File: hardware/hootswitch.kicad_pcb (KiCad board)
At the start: 2 copper layers, 100 x 88 mm, 137 parts, among them J1 Mini-DIN-4-G, J2 Switch1, J3 Mini-DIN-4-G, J4 Mini-DIN-4-G, J5 Mini-DIN-4-G, J6 Mini-DIN-4-G, J7 Barrel_Jack_MountingPin, J8 POWER, J9 POWSEL, Q1 MMBT3904, Q10 MMBT3904, Q11 MMBT3904, Q12 MMBT3904, Q13 MMBT3904, Q14 MMBT3904, Q15 MMBT3904, Q16 MMBT3904, Q17 MMBT3904, Q18 MMBT3904, Q19 MMBT3904, Q2 MMBT3904, Q20 MMBT3904, Q21 MMBT3906, Q22 MMBT3906, Q23 MMBT3906, Q24 MMBT3906, Q3 MMBT3904, Q4 MMBT3904, Q5 MMBT3904, Q6 MMBT3904, Q7 MMBT3904, Q8 MMBT3904, Q9 MMBT3904, SW1 Switch1, U1 Pico, U10 LTV-357T, U11 LTV-357T, U12 LTV-357T, U13 LTV-357T, U14 LM1117-5.0, U2 LTV-357T, U3 LTV-357T, U4 LTV-357T, U5 LTV-357T, U6 LTV-357T, U7 LTV-357T, U8 LTV-357T, U9 LTV-357T

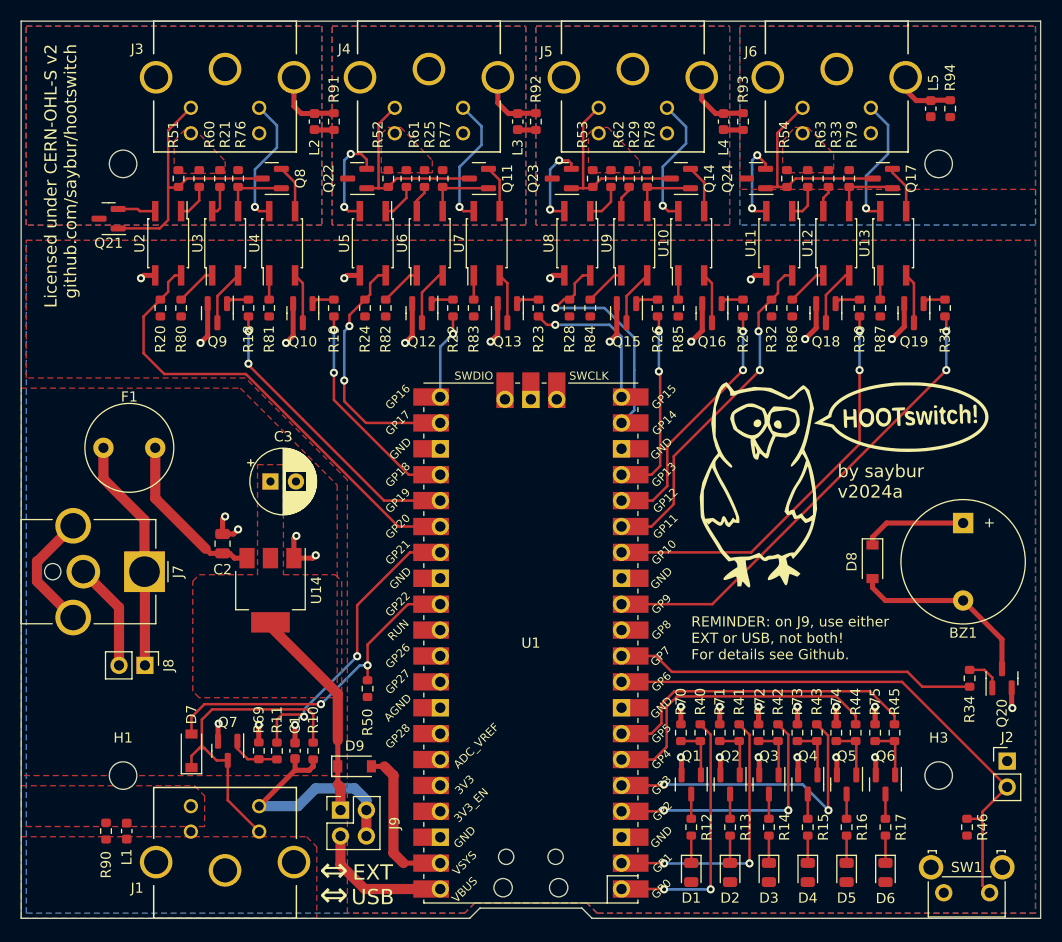
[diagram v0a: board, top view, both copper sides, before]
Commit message: Switch to using proper digital isolator for data lines.
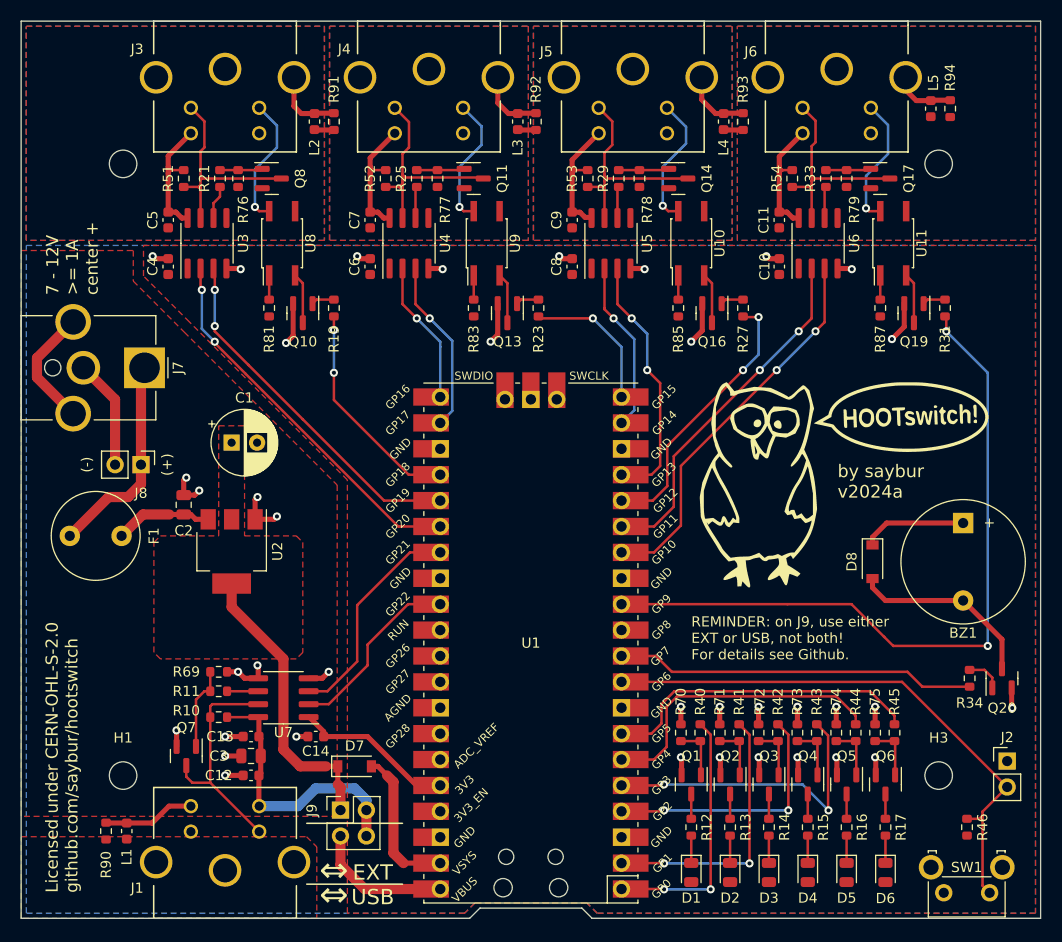
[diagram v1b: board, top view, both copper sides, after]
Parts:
- removed the D7 at (76.7, 131.6)
- removed Q12, Q15, Q18, Q9: MMBT3904, Package_TO_SOT_SMD:SOT-23
- removed Q21, Q22, Q23, Q24: MMBT3906, Package_TO_SOT_SMD:SOT-23
- removed R18, R20, R22, R24, R26, R28, R30, R32: 1K, Resistor_SMD:R_0603_1608Metric
- removed R50: 4K7, Resistor_SMD:R_0603_1608Metric
- removed R60, R61, R62, R63: 470, Resistor_SMD:R_0603_1608Metric
- removed R80, R82, R84, R86: 330, Resistor_SMD:R_0603_1608Metric
- removed the U11 at (134.4, 81.8)
- removed U12: LTV-357T, Package_SO:SO-4_4.4x3.6mm_P2.54mm
- removed the U2 at (74.4, 81.8)
- removed the U8 at (114.6, 81.8)
- removed the U9 at (120.1, 81.8)
- added C10: 100nF, Capacitor_SMD:C_0603_1608Metric, F.Cu at (134.4, 84.1)
- added C11: 100nF, Capacitor_SMD:C_0603_1608Metric, F.Cu at (134.4, 79.5)
- added C13: 100nF, Capacitor_SMD:C_0603_1608Metric, F.Cu at (82.5, 130.2)
- added C14: 100nF, Capacitor_SMD:C_0603_1608Metric, F.Cu at (88.9, 130.2)
- added C3: 10uF, Capacitor_SMD:C_0805_2012Metric, F.Cu at (82.5, 132.1)
- added C4: 100nF, Capacitor_SMD:C_0603_1608Metric, F.Cu at (74.4, 84.1)
- added C5: 100nF, Capacitor_SMD:C_0603_1608Metric, F.Cu at (74.4, 79.5)
- added C6: 100nF, Capacitor_SMD:C_0603_1608Metric, F.Cu at (94.2, 84.1)
- added C7: 100nF, Capacitor_SMD:C_0603_1608Metric, F.Cu at (94.2, 79.5)
- added C8: 100nF, Capacitor_SMD:C_0603_1608Metric, F.Cu at (114.0, 84.1)
- added C9: 100nF, Capacitor_SMD:C_0603_1608Metric, F.Cu at (114.0, 79.5)
- added U4: ADuM1201AR, Package_SO:SOIC-8_3.9x4.9mm_P1.27mm, F.Cu at (98.0, 81.8)
- added U7: ADuM1201AR, Package_SO:SOIC-8_3.9x4.9mm_P1.27mm, F.Cu at (85.7, 126.4)
- D8: value 1N4148W -> B5819W
- U3, U5, U6: value LTV-357T -> ADuM1201AR; footprint Package_SO:SO-4_4.4x3.6mm_P2.54mm -> Package_SO:SOIC-8_3.9x4.9mm_P1.27mm
- moved U6 38.1 mm to (138.2, 81.8)
- moved U5 23.4 mm to (117.9, 81.8), turned to 90 degrees
- moved J7 20.0 mm to (72.1, 94.0)
- moved J8 19.7 mm to (71.8, 103.5)
- moved R10 9.85 mm to (79.4, 128.3), turned to 180 degrees
- moved F1 9.25 mm to (64.8, 110.5)
- moved R69 8.69 mm to (79.4, 123.8), turned to 0 degrees
- moved R11 8.18 mm to (79.4, 125.7), turned to 180 degrees
- moved C1 5.39 mm to (80.6, 101.3)
- moved C2 5.39 mm to (75.9, 107.4)
- moved U2 5.39 mm to (80.6, 112.0)
- moved C12 4.95 mm to (82.5, 134.0), turned to 180 degrees
- moved Q7 4.10 mm to (76.2, 132.1)
- moved U3 1.78 mm to (78.2, 81.8)
- moved R29 1.02 mm to (118.6, 75.4)
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- renumbered C3 to C1, C1 to C12, D9 to D7, U13 to U11, U14 to U2, U4 to U8, U7 to U9
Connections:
- R11 pad 1: /A_DO -> Net-(U7-Pad6)
- R21 pad 2: Net-(J3-Pad3) -> Net-(Q8-Pad1)
- R25 pad 2: Net-(J4-Pad3) -> Net-(Q11-Pad1)
- R29 pad 2: Net-(J5-Pad3) -> Net-(Q14-Pad1)
- R33 pad 2: Net-(J6-Pad3) -> Net-(Q17-Pad1)
- U1 pad 21: /C2_DO -> /C2_DI
- U1 pad 22: /C2_DI -> /C2_DO
- U3 pad 1: Net-(R80-Pad1) -> +3.3V
- U3 pad 2: Net-(Q9-Pad3) -> /C1_DI
- U3 pad 3: Net-(Q8-Pad1) -> /C1_DO
- U3 pad 4: Net-(R21-Pad1) -> GND
- U5 pad 1: Net-(R61-Pad1) -> +3.3V
- U5 pad 2: Net-(Q22-Pad2) -> /C3_DI
- U5 pad 3: GND -> /C3_DO
- U5 pad 4: /C2_DI -> GND
- U6 pad 1: Net-(R82-Pad1) -> +3.3V
- U6 pad 2: Net-(Q12-Pad3) -> /C4_DI
- U6 pad 3: Net-(Q11-Pad1) -> /C4_DO
- U6 pad 4: Net-(R25-Pad1) -> GND
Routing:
- net /C4_PSW: track 46.7 -> 71.7 mm
- net +3.3V: track 10.2 -> 26.2 mm
- net /A_DI: track 33.3 -> 18.2 mm, vias 2 -> 0
- net Net-(J5-Pad3): track 0.00 -> 13.1 mm
- net Net-(J4-Pad3): track 0.00 -> 13.0 mm
- net Net-(J3-Pad3): track 0.00 -> 12.9 mm
- net Net-(J6-Pad3): track 0.00 -> 12.7 mm
- net /C2_DI: track 24.8 -> 14.1 mm, vias 2 -> 1
- net Net-(Q22-Pad2): track 9.87 -> 0.00 mm, vias 2 -> 0
- net Net-(J1-Pad4): track 0.00 -> 9.03 mm
- net /C2_DO: track 8.43 -> 17.1 mm
- net Net-(Q24-Pad2): track 8.60 -> 0.00 mm, vias 2 -> 0
- net Net-(U7-Pad7): track 31.3 -> 22.8 mm
- net Net-(Q23-Pad2): track 8.50 -> 0.00 mm, vias 2 -> 0
- net /C1_DI: track 45.7 -> 37.5 mm, vias 0 -> 2
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- removed copper zone on F.Cu, net Net-(J1-Pad4)
- removed copper zone on F.Cu, net Net-(J3-Pad3)
- removed copper zone on F.Cu, net Net-(J4-Pad3)
- removed copper zone on F.Cu, net Net-(J5-Pad3)
- removed copper zone on F.Cu, net Net-(J6-Pad3)
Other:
- board text added: "(+)"
- board text added: "(-)"
- board text added: "7 - 12V >= 1A center +"
- board text added: "Licensed under CERN-OHL-S-2.0 github.com/saybur/hootswitch"
- board text removed: "Licensed under CERN-OHL-S v2 github.com/saybur/hootswitch"

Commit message: Refinements for v2024a during BOM creation.
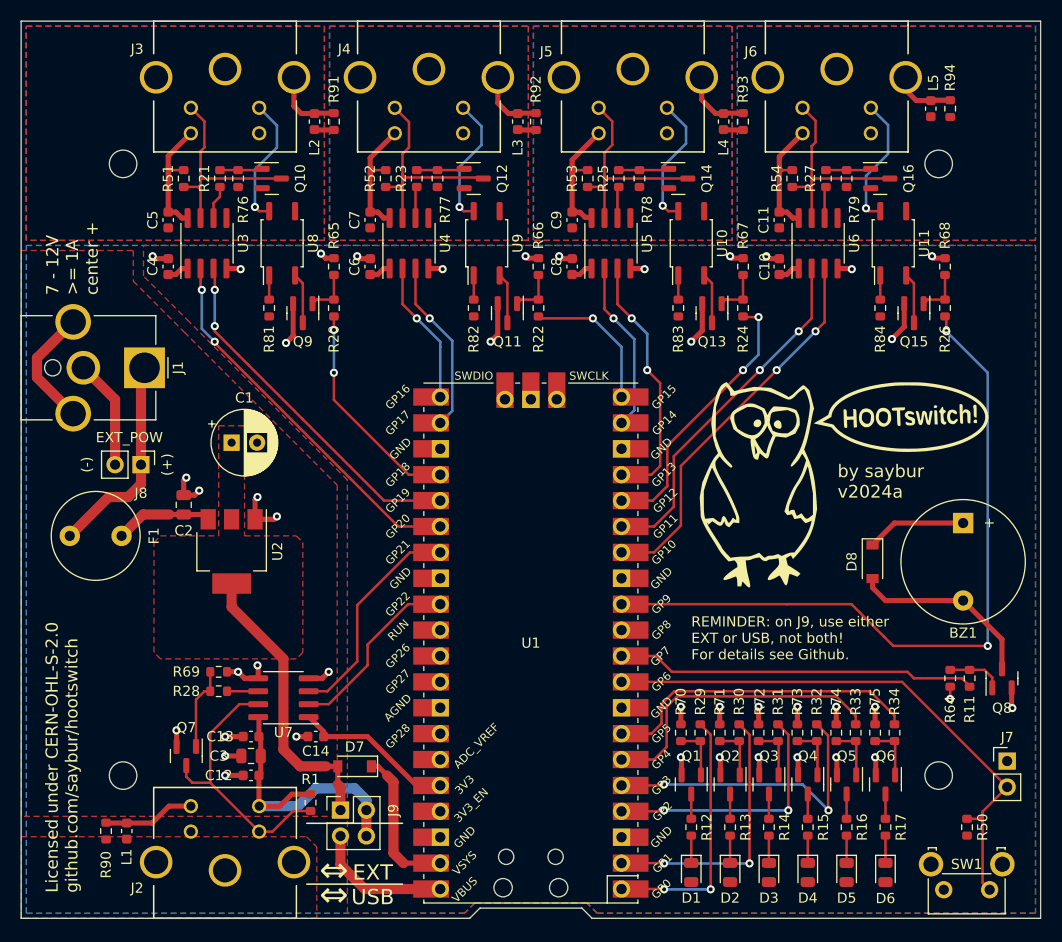
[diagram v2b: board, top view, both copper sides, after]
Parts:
- added R64: 10K, Resistor_SMD:R_0603_1608Metric, F.Cu at (151.1, 124.5)
- added R65: 10K, Resistor_SMD:R_0603_1608Metric, F.Cu at (90.7, 84.1)
- added R66: 10K, Resistor_SMD:R_0603_1608Metric, F.Cu at (110.7, 84.1)
- added R67: 10K, Resistor_SMD:R_0603_1608Metric, F.Cu at (130.8, 84.1)
- added R68: 10K, Resistor_SMD:R_0603_1608Metric, F.Cu at (150.6, 84.1)
- J8: value POWER -> EXT_POW
- L1, L2, L3, L4, L5: value 0.1uF -> DNP
- R1: renamed from R10; value 1K -> 470
- R20: renamed from R19; value 1K -> 2K2
- R21: value 1K -> 2K2
- R22: renamed from R23; value 1K -> 2K2
- R23: renamed from R25; value 1K -> 2K2
- R24: renamed from R27; value 1K -> 2K2
- R25: renamed from R29; value 1K -> 2K2
- R26: renamed from R31; value 1K -> 2K2
- R27: renamed from R33; value 1K -> 2K2
- R28: renamed from R11; value 1K -> 2K2
- R50: renamed from R46; value 2K2 -> 4K7
- R90, R91, R92, R93, R94: value 1M -> 0
- U10, U11, U8, U9: footprint Package_SO:SO-4_4.4x3.6mm_P2.54mm -> Package_SO:SO-4_4.4x3.9mm_P2.54mm
- moved R1 12.3 mm to (88.4, 136.7), turned to -90 degrees
- moved SW1 0.30 mm to (155.0, 145.2)
- turned D7 to 180 degrees
- renumbered J7 to J1, J1 to J2, J2 to J7, Q8 to Q10, Q13 to Q11, Q11 to Q12, Q16 to Q13, Q19 to Q15, Q17 to Q16, Q20 to Q8, Q10 to Q9, R34 to R11, R40 to R29, R41 to R30, R42 to R31, R43 to R32, R44 to R33, R45 to R34, R83 to R82, R85 to R83, R87 to R84
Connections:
- D7 pad 1: Net-(C1-Pad1) -> Net-(D7-Pad1)
- D7 pad 2: Net-(D7-Pad2) -> Net-(C1-Pad1)
- U1 pad 39: Net-(D7-Pad2) -> Net-(D7-Pad1)
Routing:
- net Net-(D7-Pad2): track 14.8 -> 0.00 mm
- net Net-(D7-Pad1): track 0.00 -> 14.8 mm
- net +3.3V: track 26.2 -> 34.3 mm
- net GND: track 73.4 -> 80.1 mm, vias 37 -> 42
- net Net-(J2-Pad1): track 22.8 -> 27.1 mm
- net +5V: track 27.2 -> 29.7 mm
- net Net-(Q9-Pad1): track 2.26 -> 4.68 mm
- net Net-(Q15-Pad1): track 2.26 -> 4.68 mm
- net Net-(Q13-Pad1): track 2.26 -> 4.68 mm
- net Net-(Q11-Pad1): track 2.26 -> 4.68 mm
- net Net-(Q8-Pad1): track 3.54 -> 5.44 mm

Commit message: Add TWI and second DIN connector, update BOM.
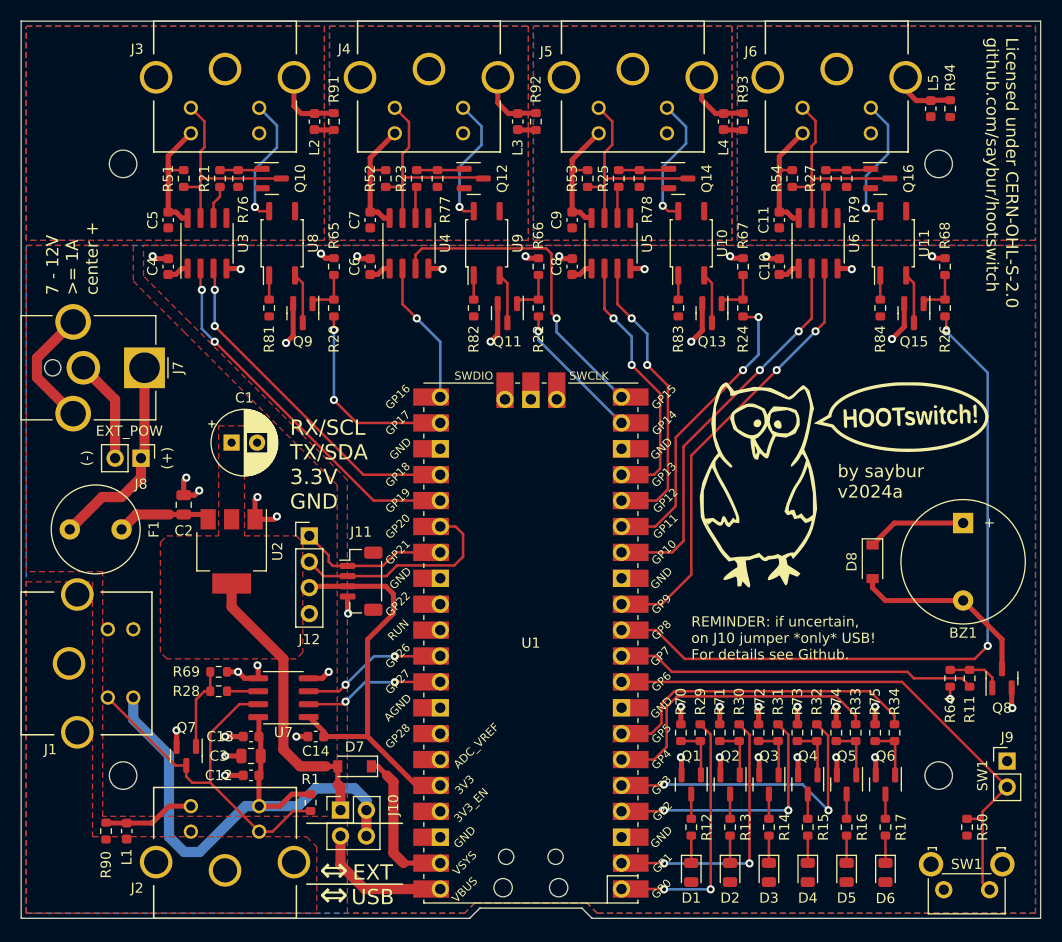
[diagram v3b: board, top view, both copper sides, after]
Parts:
- added J1: Mini-DIN-4-G, hootswitch:5749181-1, F.Cu at (60.0, 123.0)
- added J11: TWI, Connector_JST:JST_SH_BM04B-SRSS-TB_1x04-1MP_P1.00mm_Vertical, F.Cu at (93.3, 114.9)
- added J12: TWI, Connector_PinHeader_2.54mm:PinHeader_1x04_P2.54mm_Vertical, F.Cu at (88.3, 110.5)
- J9: renamed from J7; value Switch1 -> SW1
- moved F1 0.63 mm to (64.8, 109.9)
- moved J8 0.63 mm to (71.8, 102.9)
- renumbered J9 to J10, J1 to J7
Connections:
- J2 pad 4: Net-(J2-Pad4) -> GND
- L1 pad 1: Net-(J2-Pad4) -> GND
- R90 pad 1: Net-(J2-Pad4) -> GND
- U1 pad 11: unconnected-(U1-Pad11) -> /C4_PSW
- U1 pad 12: /C4_PSW -> /C4_DO
- U1 pad 14: /C4_DO -> /C4_DI
- U1 pad 15: /C4_DI -> /C3_PSW
- U1 pad 16: /C3_PSW -> /C3_DO
- U1 pad 17: /C3_DO -> /C3_DI
- U1 pad 19: /C3_DI -> /C2_PSW
- U1 pad 20: /C2_PSW -> /C2_DO
- U1 pad 22: /C2_DO -> /C1_PSW
- U1 pad 24: /C1_PSW -> /C1_DO
- U1 pad 25: /C1_DO -> /C1_DI
- U1 pad 26: /C1_DI -> Net-(U1-Pad26)
- U1 pad 27: /A_DO -> Net-(U1-Pad27)
- U1 pad 29: /A_DI -> unconnected-(U1-Pad29)
- U1 pad 31: unconnected-(U1-Pad31) -> /A_DO
- U1 pad 32: unconnected-(U1-Pad32) -> /A_DI
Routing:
- net +5V: track 29.7 -> 56.1 mm
- net +3.3V: track 34.3 -> 58.0 mm
- net Net-(U1-Pad26): track 0.00 -> 21.2 mm
- net Net-(U1-Pad27): track 0.00 -> 15.0 mm
- net /C2_DO: track 17.1 -> 32.1 mm
- net GND: track 80.1 -> 90.8 mm, vias 42 -> 43
- net Net-(J2-Pad1): track 27.1 -> 37.5 mm
- net /C3_DI: track 16.9 -> 25.9 mm, vias 1 -> 2
- net Net-(J2-Pad4): track 9.03 -> 0.00 mm
- net /A_DO: track 21.8 -> 14.3 mm, vias 0 -> 2
- net /C4_DO: track 38.0 -> 43.5 mm
- net /A_DI: track 18.2 -> 13.8 mm, vias 0 -> 2
- net /C4_DI: track 34.9 -> 38.5 mm
- net /C3_DO: track 25.3 -> 28.7 mm
- net /C3_PSW: track 26.9 -> 29.6 mm
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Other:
- board text added: "REMINDER: if uncertain, on J10 jumper *only* USB! For details see Github."
- board text added: "RX/SCL TX/SDA 3.3V GND"
- board text removed: "REMINDER: on J9, use either EXT or USB, not both! For details see Github."
